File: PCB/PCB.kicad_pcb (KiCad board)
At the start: 2 copper layers, 41 parts, among them J1 USB_C_Receptacle_USB2.0_16P, SW1 RESET, SW2 Button, U1 RP2040, U2 W25Q32JVSS

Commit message: everything is fine
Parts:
- added U3: ~, Taranium-libs:FPC-SMD_24P-P0.50_05A20L24P, F.Cu at (148.6, 76.8)
- moved C20 58.1 mm to (142.7, 72.4), turned to 180 degrees
- moved C16 56.2 mm to (142.7, 69.9), turned to 180 degrees
- moved R7 53.0 mm to (82.0, 98.8)
- moved R3 52.4 mm to (79.1, 80.1)
- moved R6 52.3 mm to (82.0, 95.0)
- moved SW1 48.0 mm to (74.6, 77.8), turned to 90 degrees
- moved C4 35.8 mm to (79.6, 59.0)
- moved C5 35.8 mm to (79.6, 60.6)
- moved C6 35.8 mm to (79.6, 62.3)
- moved C7 35.8 mm to (79.6, 64.0)
- moved U2 31.7 mm to (104.5, 92.6)
- moved R4 23.2 mm to (114.0, 88.8), turned to 90 degrees
- moved R5 21.9 mm to (115.5, 90.1)
- moved C23 20.6 mm to (132.6, 75.1), turned to 90 degrees
- moved C15 19.4 mm to (142.7, 74.0), turned to 180 degrees
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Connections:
- net BS renamed GND
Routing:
- net +3V3: track 0.00 -> 91.2 mm, vias 0 -> 2
- net Net-(U1-RUN): track 0.00 -> 37.1 mm
- net SPI_SS: track 0.00 -> 22.3 mm
- net SPI_Q1: track 0.00 -> 15.8 mm
- net VGH: track 0.00 -> 13.7 mm, vias 0 -> 2
- net SPI_Q2: track 0.00 -> 12.7 mm
- net SPI_Q3: track 0.00 -> 12.7 mm
- net GND: track 17.8 -> 5.67 mm, vias 2 -> 3
- net Net-(R5-Pad2): track 0.00 -> 11.2 mm
- net SPI_SCLK: track 0.00 -> 10.6 mm
- net Net-(U1-USB_DM): track 12.9 -> 22.7 mm
- net Net-(U1-USB_DP): track 13.4 -> 22.8 mm
- net SPI_Q0: track 0.00 -> 8.52 mm
- net +1V1: track 34.0 -> 26.1 mm, vias 2 -> 0
- net Net-(D1-K): track 0.00 -> 6.87 mm
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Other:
- board outline added: 100 x 52.9 mm
- board text added: "RESET"

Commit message: routing is fun
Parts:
- added L1: L_Small, Taranium-libs:IND-SMD_L6.0-W6.0_FNR60XXS, F.Cu at (124.6, 75.6)
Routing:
- net +3V3: track 91.2 -> 104.4 mm
- net Net-(D3-A): track 2.34 -> 8.04 mm
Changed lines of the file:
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@@
+		)
+	)
+	(footprint "Taranium-libs:IND-SMD_L6.0-W6.0_FNR60XXS"
+		(layer "F.Cu")
+		(at 124.6 75.6)
+		(property "Reference" "L1"
+			(at 0 -4.01 0)
+			(layer "F.SilkS")
+			(effects
+				(font
+					(size 1 1)
+					(thickness 0.15)
+				)
+			)
+		)
+		(property "Value" "L_Small"
+			(at 0 4.01 0)
+			(layer "F.Fab")
+			(effects
+				(font
+					(size 1 1)
+					(thickness 0.15)
+				)
+			)
+		)
+		(property "Datasheet" ""
+			(at 0 0 0)
+			(layer "F.Fab")
+			(hide yes)
+			(effects
+				(font
+					(size 1.27 1.27)
+					(thickness 0.15)
+				)
+			)
+		)
+		(property "Description" "Inductor, small symbol"
+			(at 0 0 0)
+			(layer "F.Fab")
+			(hide yes)
+			(effects
+				(font
+					(size 1.27 1.27)
+					(thickness 0.15)
+				)
+			)
+		)
+		(property ki_fp_filters "Choke_* *Coil* Inductor_* L_*")
+		(sheetname "/")
+		(sheetfile "PCB.kicad_sch")
+		(attr smd)
+		(fp_line
+			(start -1.69 -3)
+			(end 1.67 -3)
+			(stroke
+				(width 0.25)
+				(type solid)
+			)
+			(layer "F.SilkS")
+		)
+		(fp_line
+			(start -1.67 3)
+			(end 1.69 3)
+			(stroke
+				(width 0.25)
+				(type solid)
+			)
+			(layer "F.SilkS")
+		)
+		(fp_circle
+			(center -3 -3)
+			(end -2.97 -3)
+			(stroke
+				(width 0.06)
+				(type solid)
+			)
+			(fill no)
+			(layer "F.Fab")
+		)
+		(fp_text user "${REFERENCE}"
+			(at 0 0 0)
+			(layer "F.Fab")
+			(effects
+				(font
+					(size 1 1)
+					(thickness 0.15)
+				)
+			)
+		)
+		(pad "1" smd rect
+			(at -2.35 0.01)
+			(size 2.5 5.7)
+			(layers "F.Cu" "F.Mask" "F.Paste")
+			(net 3 "+3V3")
+			(pintype "passive")
+		)
+		(pad "2" smd rect
+			(at 2.35 -0.01)
+			(size 2.5 5.7)
+			(layers "F.Cu" "F.Mask" "F.Paste")
+			(net 13 "Net-(D3-A)")
+			(pintype "passive")
+		)
+		(embedded_fonts no)
+		(model "${EASYEDA2KICAD}/easyeda2kicad.3dshapes/IND-SMD_L6.0-W6.0-H2.8.wrl"
+			(offset
+				(xyz 0 -0 -0)
+			)
+			(scale
+				(xyz 1 1 1)
+			)
+			(rotate
+				(xyz 0 0 270)
+			)
 		)
 	)
@@
 	)
 	(segment
+		(start 122.25 79.149)
+		(end 115.3995 85.9995)
+		(width 0.4)
+		(layer "F.Cu")
+		(net 3)
+	)
+	(segment
 		(start 115.799 85.6)
 		(end 135.5 85.6)
@@
 	)
 	(segment
-		(start 113 88.399)
+		(start 115.3995 85.9995)
 		(end 115.799 85.6)
 		(width 0.4)
@@
 	)
 	(segment
+		(start 122.25 75.61)
+		(end 122.25 79.149)
+		(width 0.4)
+		(layer "F.Cu")
+		(net 3)
+	)
+	(segment
 		(start 103.954416 84.3)
 		(end 103.81158 84.157164)
+		(width 0.4)
+		(layer "F.Cu")
+		(net 3)
+	)
+	(segment
+		(start 113 88.399)
+		(end 115.3995 85.9995)
 		(width 0.4)
 		(layer "F.Cu")
@@
 		(width 0.2)
 		(layer "F.Cu")
+		(net 13)
+	)
+	(segment
+		(start 132.31 75.59)
+		(end 132.55 75.35)
+		(width 0.2)
+		(layer "F.Cu")
+		(net 13)
+	)
+	(segment
+		(start 126.95 75.59)
+		(end 132.31 75.59)
+		(width 0.2)
+		(layer "F.Cu")

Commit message: amongus vias arent real, they cant hurt you. amongus vias:
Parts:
- added Q1: NMOS, Package_TO_SOT_SMD:SOT-23, F.Cu at (135.4, 82.1)
- moved C6 30.5 mm to (107.3, 74.8)
- moved C9 29.6 mm to (106.3, 85.3)
- moved C7 29.3 mm to (106.5, 75.6)
- moved C4 27.3 mm to (97.0, 80.0), turned to -90 degrees
- moved C5 24.8 mm to (99.5, 75.4), turned to 180 degrees
- moved C8 24.1 mm to (105.6, 84.6)
- moved C10 23.6 mm to (95.7, 80.0), turned to -90 degrees
- moved C11 22.2 mm to (95.0, 79.4), turned to 90 degrees
- moved C12 20.0 mm to (96.4, 79.4), turned to 90 degrees
- moved L1 11.2 mm to (127.0, 64.7)
- moved D3 9.00 mm to (136.2, 67.9)
- moved C23 7.93 mm to (132.3, 67.2)
- moved D2 7.51 mm to (136.3, 65.4)
- moved D1 5.91 mm to (136.3, 62.8)
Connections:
- D1 pad 2: unconnected-(D1-A-Pad2) -> VGL
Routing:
- net +3V3: track 104.4 -> 171.1 mm, vias 2 -> 5
- net GND: track 5.67 -> 49.5 mm, vias 3 -> 17
- net +1V1: track 26.1 -> 47.8 mm, vias 0 -> 3
- net GDR: track 5.14 -> 17.7 mm
- net Net-(D3-A): track 8.04 -> 19.8 mm
- net VGL: track 4.79 -> 16.3 mm
- net RESE: track 4.69 -> 11.9 mm
- net Net-(D1-K): track 6.87 -> 5.60 mm
- net VGH: track 13.7 -> 13.0 mm
- net Net-(U1-RUN): track 37.1 -> 37.3 mm, vias 0 -> 2
- added copper zone on B.Cu, net GND
- added copper zone on F.Cu, net GND

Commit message: descriptive commit name
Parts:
- added C22: 10uF, Capacitor_SMD:C_01005_0402Metric, F.Cu at (81.8, 89.5)
- added C24: 10uF, Capacitor_SMD:C_01005_0402Metric, F.Cu at (79.5, 84.6)
- added C25: 33pF, Capacitor_SMD:C_01005_0402Metric, F.Cu at (110.7, 72.5)
- added C26: 33pF, Capacitor_SMD:C_01005_0402Metric, F.Cu at (107.9, 75.9)
- added R11: 1k, Resistor_SMD:R_01005_0402Metric, F.Cu at (108.7, 72.7)
- added U4: NCP1117-3.3_SOT223, Package_TO_SOT_SMD:SOT-223-3_TabPin2, F.Cu at (84.7, 84.3)
- added Y1: 12 MHz, Taranium-libs:CRYSTAL-SMD_4P-L3.2-W2.5-BL, F.Cu at (110.8, 74.7)
- moved C1 1.73 mm to (97.2, 100.2)
- moved C10 1.73 mm to (94.8, 78.5)
- moved C11 1.73 mm to (94.1, 77.9)
- moved C12 1.73 mm to (95.5, 77.9)
- moved C13 1.73 mm to (141.6, 79.0)
- moved C15 1.73 mm to (141.8, 72.5)
- moved C19 1.73 mm to (141.8, 71.7)
- moved C23 1.73 mm to (131.4, 65.7)
- moved C3 1.73 mm to (91.6, 100.1)
- moved C4 1.73 mm to (96.1, 78.5)
- moved D2 1.73 mm to (135.4, 63.9)
- moved J1 1.73 mm to (74.2, 95.1)
- moved L1 1.73 mm to (126.1, 63.2)
- moved R1 1.73 mm to (83.0, 96.0)
- moved R10 1.73 mm to (75.3, 86.4)
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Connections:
- J1 pad A4: +3V3 -> VBUS
- J1 pad A9: +3V3 -> VBUS
- J1 pad B4: +3V3 -> VBUS
- J1 pad B9: +3V3 -> VBUS
- U1 pad 12: unconnected-(U1-GPIO9-Pad12) -> SDA
- U1 pad 13: unconnected-(U1-GPIO10-Pad13) -> SCL
- U3 pad 13: SCLK -> SCL
- U3 pad 14: SDI -> SDA
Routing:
- net VBUS: track 0.00 -> 15.4 mm, vias 0 -> 2
- net GND: track 49.5 -> 63.9 mm, vias 17 -> 64
- net XOUT: track 0.00 -> 5.94 mm
- net +3V3: track 171.1 -> 165.5 mm
- net XIN: track 0.00 -> 5.54 mm
- net Net-(C25-Pad2): track 0.00 -> 3.48 mm
- net Net-(D3-A): track 19.8 -> 20.0 mm, vias 0 -> 2
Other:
- board size 100 x 52.9 mm -> 100 x 53 mm

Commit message: push
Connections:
- C1 pad 2: GND -> BS
- C10 pad 2: GND -> BS
- C11 pad 2: GND -> BS
- C12 pad 2: GND -> BS
- C13 pad 2: GND -> BS
- C14 pad 2: GND -> BS
- C15 pad 2: GND -> BS
- C16 pad 2: GND -> BS
- C17 pad 2: GND -> BS
- C18 pad 2: GND -> BS
- C19 pad 2: GND -> BS
- C2 pad 2: GND -> BS
- C20 pad 2: GND -> BS
- C21 pad 1: GND -> BS
- C22 pad 2: GND -> BS
- C24 pad 2: GND -> BS
- C25 pad 1: GND -> BS
- C26 pad 1: GND -> BS
- C3 pad 2: GND -> BS
- C4 pad 2: GND -> BS
- C5 pad 2: GND -> BS
- C6 pad 2: GND -> BS
- C7 pad 2: GND -> BS
- C8 pad 2: GND -> BS
- C9 pad 2: GND -> BS
- D2 pad 1: GND -> BS
- D4 pad 1: GND -> BS
- J1 pad A1: GND -> BS
- J1 pad A12: GND -> BS
- J1 pad B1: GND -> BS
- J1 pad B12: GND -> BS
- J1 pad S1: GND -> BS
- R6 pad 2: GND -> BS
- R7 pad 2: GND -> BS
- R8 pad 1: GND -> BS
- R9 pad 1: GND -> BS
- SW1 pad 1: GND -> BS
- SW2 pad 1: GND -> BS
- U1 pad 11: unconnected-(U1-GPIO8-Pad11) -> CS
- U1 pad 19: GND -> BS
- U1 pad 57: GND -> BS
- U1 pad 6: unconnected-(U1-GPIO4-Pad6) -> BS
- U1 pad 7: unconnected-(U1-GPIO5-Pad7) -> BUSY
- U1 pad 8: unconnected-(U1-GPIO6-Pad8) -> RES
- U1 pad 9: unconnected-(U1-GPIO7-Pad9) -> D/C
- U2 pad 4: GND -> BS
- U3 pad 8: GND -> BS
- U3 pad MP: GND -> BS
- U4 pad 1: GND -> BS
- Y1 pad 2: GND -> BS
- Y1 pad 4: GND -> BS
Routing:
- net BS: track 0.00 -> 66.3 mm, vias 0 -> 64
- net GND: track 63.9 -> 0.00 mm, vias 64 -> 0
- net BUSY: track 0.00 -> 45.5 mm
- net D/C: track 0.00 -> 44.9 mm
- net RES: track 0.00 -> 44.7 mm
- net SDA: track 0.00 -> 43.3 mm
- net CS: track 0.00 -> 43.3 mm
- net SCL: track 0.00 -> 42.8 mm, vias 0 -> 2
- net +3V3: track 165.5 -> 170.8 mm, vias 5 -> 6
- added copper zone on B.Cu, net BS
- added copper zone on F.Cu, net BS
- removed copper zone on B.Cu, net GND
- removed copper zone on F.Cu, net GND

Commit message: potato
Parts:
- removed C15: 1uF, Capacitor_SMD:C_01005_0402Metric
- C1, C10, C11, C12, C13, C14, C16, C17, C18, C19, C2, C20, C21, C22, C23, C24, C25, C26, C3, C4, C5, C6, C7, C8, C9: footprint Capacitor_SMD:C_01005_0402Metric -> Capacitor_SMD:C_0402_1005Metric
- R1, R10, R11, R2, R3, R4, R5, R6, R7, R8, R9: footprint Resistor_SMD:R_01005_0402Metric -> Resistor_SMD:R_0402_1005Metric
- moved C16 3.10 mm to (144.9, 68.3), turned to 90 degrees
- moved C17 2.16 mm to (143.8, 68.4), turned to 90 degrees
- moved C18 1.78 mm to (141.9, 68.3), turned to 90 degrees
- moved C11 1.63 mm to (92.5, 77.6)
- moved C10 1.31 mm to (93.5, 78.7)
- moved C12 0.93 mm to (94.6, 77.6)
- moved C25 0.81 mm to (110.6, 71.7)
- moved C20 0.67 mm to (141.6, 70.3)
- moved C4 0.43 mm to (95.7, 78.7)
- moved C19 0.35 mm to (141.6, 71.4)
- moved C6 0.35 mm to (106.7, 73.1)
- moved R2 0.22 mm to (83.0, 94.9)
- moved C22 0.15 mm to (82.0, 89.5)
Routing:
- net BS: track 66.3 -> 81.7 mm, vias 64 -> 149
- net Net-(U3-VDD): track 4.51 -> 0.00 mm
- net VCOM: track 4.92 -> 1.92 mm
- net VGL: track 16.3 -> 14.3 mm
- net VGH: track 13.0 -> 11.5 mm, vias 2 -> 0
- net Net-(U3-VSL): track 4.63 -> 5.29 mm
- net +1V1: track 47.8 -> 48.4 mm
- net RESE: track 11.9 -> 11.4 mm

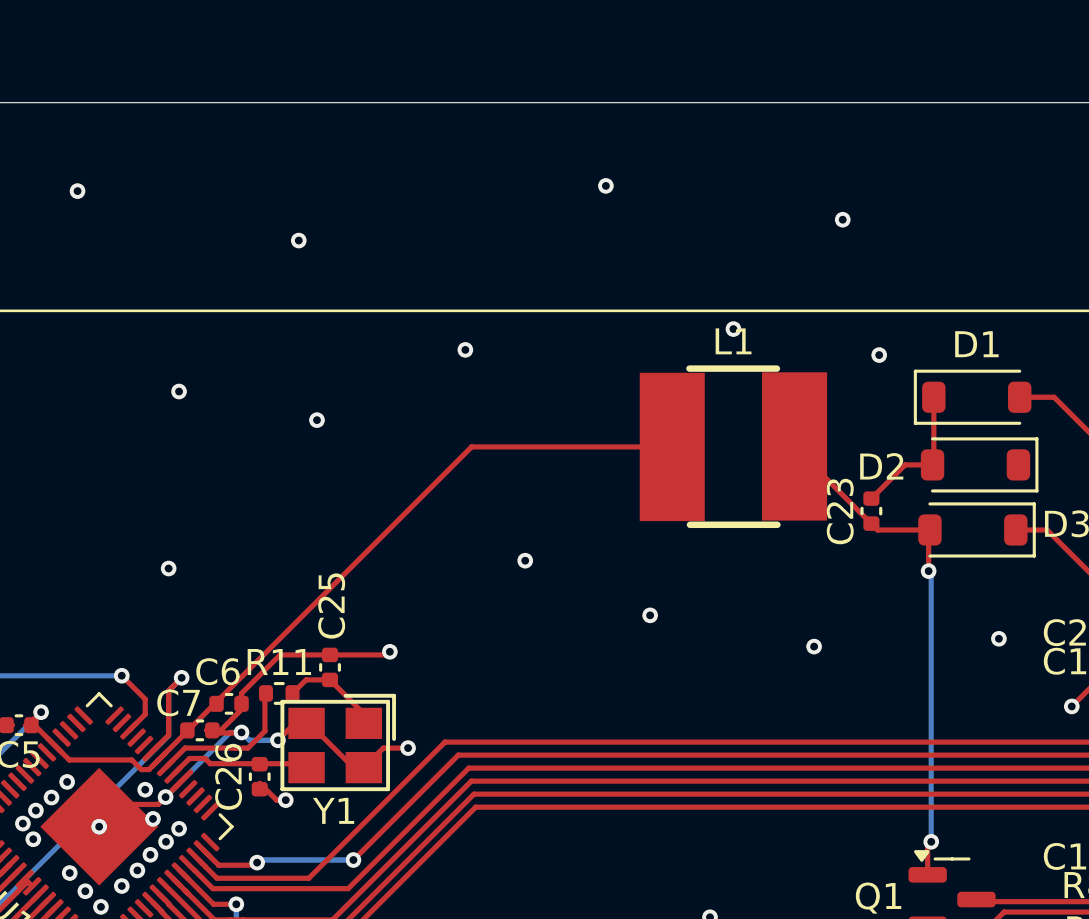
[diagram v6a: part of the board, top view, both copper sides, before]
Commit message: lanyard hole
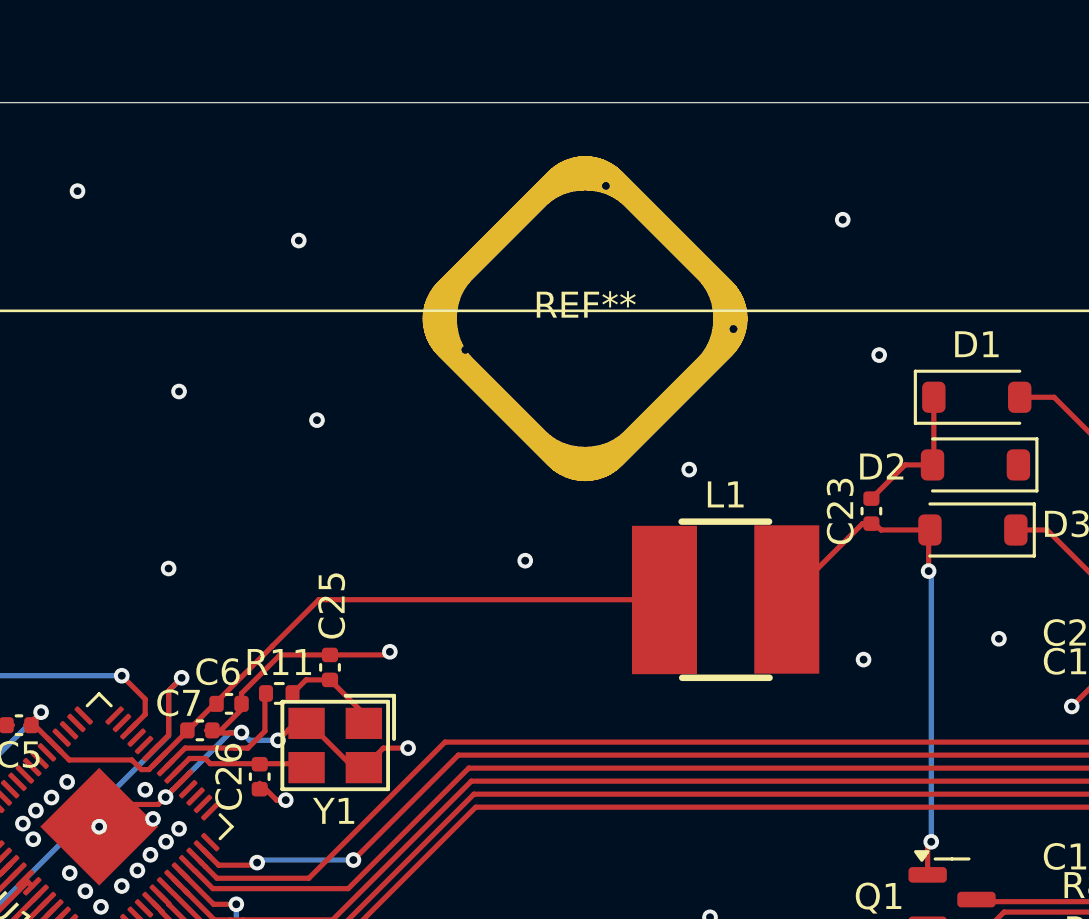
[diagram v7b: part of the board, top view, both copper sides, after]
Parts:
- added REF**: Lanyard_hole2, Taranium-libs:Lanyard_hole2, F.Cu at (120.4, 58.3)
- moved L1 5.89 mm to (125.8, 69.1)
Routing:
- net +3V3: track 170.7 -> 168.0 mm
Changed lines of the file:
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@@
 		)
 	)
+	(footprint "Taranium-libs:Lanyard_hole2"
+		(layer "F.Cu")
+		(at 120.4 58.3)
+		(property "Reference" "REF**"
+			(at 0 -0.5 0)
+			(unlocked yes)
+			(layer "F.SilkS")
+			(effects
+				(font
+					(size 1 1)
+					(thickness 0.1)
+				)
+			)
+		)
+		(property "Value" "Lanyard_hole2"
+			(at 0 1 0)
+			(unlocked yes)
+			(layer "F.Fab")
+			(effects
+				(font
+					(size 1 1)
+					(thickness 0.15)
+				)
+			)
+		)
+		(property "Datasheet" ""
+			(at 0 0 0)
+			(unlocked yes)
+			(layer "F.Fab")
+			(hide yes)
+			(effects
+				(font
+					(size 1 1)
+					(thickness 0.15)
+				)
+			)
+		)
+		(property "Description" ""
+			(at 0 0 0)
+			(unlocked yes)
+			(layer "F.Fab")
+			(hide yes)
+			(effects
+				(font
+					(size 1 1)
+					(thickness 0.15)
+				)
+			)
+		)
+		(attr smd)
+		(fp_text user "${REFERENCE}"
+			(at 0 2.5 0)
+			(unlocked yes)
+			(layer "F.Fab")
+			(effects
+				(font
+					(size 1 1)
+					(thickness 0.15)
+				)
+			)
+		)
+		(pad "1" thru_hole rect
+			(at -1.5 -1.5 45)
+			(size 2 3)
+			(drill oval 8 4)
+			(layers "*.Cu" "F.Mask" "F.Paste")
+			(remove_unused_layers no)
+		)
+		(pad "1" thru_hole rect
+			(at -1.5 1.5 135)
+			(size 2 3)
+			(drill oval 8 4)
+			(layers "*.Cu" "F.Mask" "F.Paste")
+			(remove_unused_layers no)
+		)
+		(pad "1" thru_hole roundrect
+			(at 0 0 45)
+			(size 10 10)
+			(drill 3)
+			(layers "*.Cu" "F.Mask" "F.Paste")
+			(remove_unused_layers no)
+			(roundrect_rratio 0.2)
+		)
+		(pad "1" thru_hole roundrect
+			(at 0 0 315)
+			(size 10 10)
+			(drill 3)
+			(layers "*.Cu" "B.Mask" "B.Paste")
+			(remove_unused_layers no)
+			(roundrect_rratio 0.2)
+		)
+		(pad "1" thru_hole rect
+			(at 1.5 -1.5 135)
+			(size 2 3)
+			(drill oval 8 4)
+			(layers "*.Cu" "F.Mask" "F.Paste")
+			(remove_unused_layers no)
+		)
+		(pad "1" thru_hole rect
+			(at 1.5 1.5 45)
+			(size 2 3)
+			(drill oval 8 4)
+			(layers "*.Cu" "F.Mask" "F.Paste")
+			(remove_unused_layers no)
+		)
+		(embedded_fonts no)
+	)
 	(footprint "Resistor_SMD:R_0402_1005Metric"
 		(layer "F.Cu")
@@
 	(footprint "Taranium-libs:IND-SMD_L6.0-W6.0_FNR60XXS"
 		(layer "F.Cu")
-		(at 126.1 63.22)
+		(at 125.8 69.1)
 		(property "Reference" "L1"
 			(at 0 -4.01 0)
@@
 		)
 	)
+	(dimension
+		(type orthogonal)
+		(layer "F.Cu")
+		(pts
+			(xy 120 50) (xy 120 103)
+		)
+		(height 57.9)
+		(orientation 1)
+		(format
+			(prefix "")
+			(suffix "")
+			(units 3)
+			(units_format 0)
+			(precision 4)
+			(suppress_zeroes yes)
+		)
+		(style
+			(thickness 0.2)
+			(arrow_length 1.27)
+			(text_position_mode 0)
+			(arrow_direction outward)
+			(extension_height 0.58642)
+			(extension_offset 0.5)
+			(keep_text_aligned yes)
+		)
+		(gr_text "53"
+			(at 176.1 76.5 90)
+			(layer "F.Cu")
+			(effects
+				(font
+					(size 1.5 1.5)
+					(thickness 0.3)
+				)
+			)
+		)
+	)
 	(segment
 		(start 97.25 82.584214)
@@
 	)
 	(segment
-		(start 116.038528 63.23)
+		(start 108.384264 70.884264)
 		(end 104.020629 75.247899)
 		(width 0.2)
@@
 	)
 	(segment
-		(start 123.75 63.23)
-		(end 116.038528 63.23)
-		(width 0.2)
-		(layer "F.Cu")
-		(net 2)
-	)
-	(segment
 		(start 89.6 78.62)
 		(end 78.685 78.62)
@@
 	)
 	(segment
+		(start 110.169528 69.099)
+		(end 108.384264 70.884264)
+		(width 0.2)
+		(layer "F.Cu")
+		(net 2)
+	)
+	(segment
 		(start 96.519012 78.171)
 		(end 97.462214 77.227798)
@@
 	)
 	(segment
+		(start 123.45 69.11)
+		(end 123.439 69.099)
+		(width 0.2)
+		(layer "F.Cu")
+		(net 2)
+	)
+	(segment
 		(start 107 80.801)
 		(end 106.126584 80.801)
@@
 	)
 	(segment
+		(start 123.439 69.099)
+		(end 110.169528 69.099)
+		(width 0.2)
+		(layer "F.Cu")
+		(net 2)
+	)
+	(segment
 		(start 100.0125 94.0325)
 		(end 100.6 94.62)
@@
 	)
 	(segment
+		(start 131.065 66.175)
+		(end 131.4 66.175)
+		(width 0.2)
+		(layer "F.Cu")
+		(net 12)
+	)
+	(segment
+		(start 128.15 69.09)
+		(end 131.065 66.175)
+		(width 0.2)
+		(layer "F.Cu")
+		(net 12)
+	)
+	(segment
 		(start 133.65 79.5825)
 		(end 133.5625 79.67)
@@
 	)
 	(segment
-		(start 128.45 63.228824)
-		(end 128.45 63.21)
+		(start 131.4 66.175)
+		(end 131.525 66.175)
 		(width 0.2)
 		(layer "F.Cu")
@@
 	)
 	(segment
-		(start 133.6 66.47)
-		(end 133.65 66.42)
+		(start 131.525 66.175)
+		(end 131.77 66.42)
 		(width 0.2)
 		(layer "F.Cu")
@@
 	)
 	(segment
-		(start 133.5625 79.67)
-		(end 133.5625 78.5375)
+		(start 131.77 66.42)
+		(end 133.65 66.42)
 		(width 0.2)
 		(layer "F.Cu")
@@
 	)
 	(segment
-		(start 131.641176 66.42)
-		(end 128.45 63.228824)
+		(start 133.6 66.47)
+		(end 133.65 66.42)
 		(width 0.2)
 		(layer "F.Cu")
@@
 	)
 	(segment
-		(start 133.65 66.42)
-		(end 131.641176 66.42)
+		(start 133.5625 79.67)
+		(end 133.5625 78.5375)
 		(width 0.2)
 		(layer "F.Cu")
@@
 	)
 	(via
-		(at 129.2 70.9)
+		(at 131.1 71.4)
 		(size 0.6)
 		(drill 0.3)
@@
 	)
 	(via
-		(at 122.9 69.7)
+		(at 124.4 64.1)
 		(size 0.6)
 		(drill 0.3)

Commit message: commit
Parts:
- added C15: 1uF, Capacitor_SMD:C_0402_1005Metric, F.Cu at (141.7, 72.6)
- C21, C23: footprint Capacitor_SMD:C_0402_1005Metric -> Capacitor_SMD:C_0603_1608Metric
- C22, C24: footprint Capacitor_SMD:C_0402_1005Metric -> Capacitor_SMD:C_0805_2012Metric
- R1, R2: value 22 -> 27
- moved SW1 33.2 mm to (97.7, 99.2), turned to 0 degrees
- moved C3 30.2 mm to (104.3, 72.7), turned to 135 degrees
- moved R3 24.6 mm to (94.9, 96.6), turned to 90 degrees
- moved C21 19.8 mm to (120.4, 70.0), turned to 90 degrees
- moved C12 17.2 mm to (99.5, 94.1), turned to 180 degrees
- moved C1 16.4 mm to (97.2, 83.8)
- moved C2 16.0 mm to (95.8, 84.2)
- moved U4 11.6 mm to (77.4, 75.3)
- moved REF** 10.3 mm to (120.5, 48.0)
- moved C11 2.20 mm to (94.7, 77.6)
- moved C22 1.24 mm to (81.2, 90.4)
- moved C9 0.62 mm to (105.8, 84.3)
- moved C24 0.60 mm to (78.9, 84.6)
- moved R11 0.40 mm to (108.7, 72.3)
- moved C10 0.20 mm to (93.7, 78.7)
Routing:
- net +3V3: track 168.0 -> 146.6 mm
- net +1V1: track 48.4 -> 27.5 mm
- net VBUS: track 15.4 -> 31.2 mm
- net BS: track 81.7 -> 73.2 mm
- net Net-(U3-VDD): track 0.00 -> 4.32 mm
- net Net-(U1-RUN): track 37.3 -> 40.5 mm
- net XOUT: track 5.52 -> 6.24 mm
- net SPI_Q1: track 15.8 -> 15.3 mm
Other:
- board size 100 x 53 mm -> 100 x 63 mm
